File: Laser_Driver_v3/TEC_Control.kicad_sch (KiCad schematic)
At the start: 49 parts, among them Q10 IRF9540N, Q11 IRLB8721PBF, Q12 IRF9540N, Q13 IRLB8721PBF, Q14 IRF9540N, Q7 IRLB8721PBF, Q8 IRF9540N, Q9 IRLB8721PBF, U18 OPA192, U19 OPA192, U20 OPA192, U21 OPA551U, U22 OPA551U

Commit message: Update names, footprints, values, and created BOM
Updated files names, foot prints, component values, parts.
Assigned values from Digikey catalog.
Created CSV BOMs for each schematic.
Including a Power analysis now for all components.
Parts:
- R44, R45, R46, R47, R48, R49, R50, R51, R52, R53, R54, R55, R56, R57, R58, R60: footprint Resistor_SMD:R_0402_1005Metric -> Resistor_SMD:R_0805_2012Metric_Pad1.20x1.40mm_HandSolder
- U18, U19, U20: value OPA192 -> OPA192IDR; footprint Package_SO:SOIC-5-6_4.4x3.6mm_P1.27mm -> Package_SO:SOIC-8_3.9x4.9mm_P1.27mm
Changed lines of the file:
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@@
 			)
 		)
-		(property "Footprint" "Resistor_SMD:R_0402_1005Metric"
+		(property "Footprint" "Resistor_SMD:R_0805_2012Metric_Pad1.20x1.40mm_HandSolder"
 			(at 124.46 140.97 0)
 			(hide yes)
@@
 			)
 		)
-		(property "Footprint" "Resistor_SMD:R_0402_1005Metric"
+		(property "Footprint" "Resistor_SMD:R_0805_2012Metric_Pad1.20x1.40mm_HandSolder"
 			(at 138.43 43.18 0)
 			(hide yes)
@@
 			)
 		)
-		(property "Footprint" "Resistor_SMD:R_0402_1005Metric"
+		(property "Footprint" "Resistor_SMD:R_0805_2012Metric_Pad1.20x1.40mm_HandSolder"
 			(at 124.46 120.65 0)
 			(hide yes)
@@
 			)
 		)
-		(property "Footprint" "Resistor_SMD:R_0402_1005Metric"
+		(property "Footprint" "Resistor_SMD:R_0805_2012Metric_Pad1.20x1.40mm_HandSolder"
 			(at 101.6 57.15 0)
 			(hide yes)
@@
 			)
 		)
-		(property "Footprint" "Resistor_SMD:R_0402_1005Metric"
+		(property "Footprint" "Resistor_SMD:R_0805_2012Metric_Pad1.20x1.40mm_HandSolder"
 			(at 171.45 60.96 0)
 			(hide yes)
@@
 			)
 		)
-		(property "Footprint" "Resistor_SMD:R_0402_1005Metric"
+		(property "Footprint" "Resistor_SMD:R_0805_2012Metric_Pad1.20x1.40mm_HandSolder"
 			(at 124.46 134.62 0)
 			(hide yes)
@@
 			)
 		)
-		(property "Footprint" "Resistor_SMD:R_0402_1005Metric"
+		(property "Footprint" "Resistor_SMD:R_0805_2012Metric_Pad1.20x1.40mm_HandSolder"
 			(at 87.63 134.62 0)
 			(hide yes)
@@
 			)
 		)
-		(property "Value" "OPA192"
+		(property "Value" "OPA192IDR"
 			(at 63.5 129.794 0)
 			(show_name no)
@@
 			)
 		)
-		(property "Footprint" "Package_SO:SOIC-5-6_4.4x3.6mm_P1.27mm"
+		(property "Footprint" "Package_SO:SOIC-8_3.9x4.9mm_P1.27mm"
 			(at 78.486 117.094 0)
 			(hide yes)
@@
 			)
 		)
-		(property "Footprint" "Resistor_SMD:R_0402_1005Metric"
+		(property "Footprint" "Resistor_SMD:R_0805_2012Metric_Pad1.20x1.40mm_HandSolder"
 			(at 114.3 163.83 0)
 			(hide yes)
@@
 			)
 		)
-		(property "Footprint" "Resistor_SMD:R_0402_1005Metric"
+		(property "Footprint" "Resistor_SMD:R_0805_2012Metric_Pad1.20x1.40mm_HandSolder"
 			(at 138.43 49.53 0)
 			(hide yes)
@@
 			)
 		)
-		(property "Value" "OPA192"
+		(property "Value" "OPA192IDR"
 			(at 77.47 52.324 0)
 			(show_name no)
@@
 			)
 		)
-		(property "Footprint" "Package_SO:SOIC-5-6_4.4x3.6mm_P1.27mm"
+		(property "Footprint" "Package_SO:SOIC-8_3.9x4.9mm_P1.27mm"
 			(at 92.456 39.624 0)
 			(hide yes)
@@
 			)
 		)
-		(property "Footprint" "Resistor_SMD:R_0402_1005Metric"
+		(property "Footprint" "Resistor_SMD:R_0805_2012Metric_Pad1.20x1.40mm_HandSolder"
 			(at 128.27 86.36 0)
 			(hide yes)
@@
 			)
 		)
-		(property "Footprint" "Resistor_SMD:R_0402_1005Metric"
+		(property "Footprint" "Resistor_SMD:R_0805_2012Metric_Pad1.20x1.40mm_HandSolder"
 			(at 138.43 57.15 0)
 			(hide yes)
@@
 			)
 		)
-		(property "Footprint" "Resistor_SMD:R_0402_1005Metric"
+		(property "Footprint" "Resistor_SMD:R_0805_2012Metric_Pad1.20x1.40mm_HandSolder"
 			(at 100.33 163.83 0)
 			(hide yes)
@@
 			)
 		)
-		(property "Footprint" "Resistor_SMD:R_0402_1005Metric"
+		(property "Footprint" "Resistor_SMD:R_0805_2012Metric_Pad1.20x1.40mm_HandSolder"
 			(at 114.3 86.36 0)
 			(hide yes)
@@
 			)
 		)
-		(property "Footprint" "Resistor_SMD:R_0402_1005Metric"
+		(property "Footprint" "Resistor_SMD:R_0805_2012Metric_Pad1.20x1.40mm_HandSolder"
 			(at 157.48 138.43 0)
 			(hide yes)
@@
 			)
 		)
-		(property "Value" "OPA192"
+		(property "Value" "OPA192IDR"
 			(at 43.18 82.804 0)
 			(show_name no)
@@
 			)
 		)
-		(property "Footprint" "Package_SO:SOIC-5-6_4.4x3.6mm_P1.27mm"
+		(property "Footprint" "Package_SO:SOIC-8_3.9x4.9mm_P1.27mm"
 			(at 58.166 70.104 0)
 			(hide yes)
@@
 			)
 		)
-		(property "Footprint" "Resistor_SMD:R_0402_1005Metric"
+		(property "Footprint" "Resistor_SMD:R_0805_2012Metric_Pad1.20x1.40mm_HandSolder"
 			(at 138.43 63.5 0)
 			(hide yes)
@@
 			)
 		)
-		(property "Footprint" "Resistor_SMD:R_0402_1005Metric"
+		(property "Footprint" "Resistor_SMD:R_0805_2012Metric_Pad1.20x1.40mm_HandSolder"
 			(at 124.46 127 0)
 			(hide yes)

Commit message: Clearing ERC errors. laying out components.
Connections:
- net +6V_TEC: now also Q13.2 (D)
- net -6V_TEC: now also Q14.3 (S)
- net at Q13.1 (G), R54.2: now also D21.2 (A)
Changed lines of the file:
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@@
+	)
+	(junction
+		(at 200.66 40.64)
+		(diameter 0)
+		(color 0 0 0 0)
+	)
+	(junction
+		(at 200.66 76.2)
+		(diameter 0)
+		(color 0 0 0 0)
 	)
 	(junction
@@
 	)
 	(junction
+		(at 213.36 49.53)
+		(diameter 0)
+		(color 0 0 0 0)
+	)
+	(junction
 		(at 118.11 127)
 		(diameter 0)
@@
 	)
 	(junction
+		(at 160.02 153.67)
+		(diameter 0)
+		(color 0 0 0 0)
+	)
+	(junction
+		(at 195.58 127)
+		(diameter 0)
+		(color 0 0 0 0)
+	)
+	(junction
+		(at 160.02 118.11)
+		(diameter 0)
+		(color 0 0 0 0)
+	)
+	(junction
+		(at 186.69 134.62)
+		(diameter 0)
+		(color 0 0 0 0)
+	)
+	(junction
+		(at 73.66 149.86)
+		(diameter 0)
+		(color 0 0 0 0)
+	)
+	(junction
+		(at 135.89 127)
+		(diameter 0)
+		(color 0 0 0 0)
+	)
+	(junction
+		(at 144.78 134.62)
+		(diameter 0)
+		(color 0 0 0 0)
+	)
+	(junction
+		(at 149.86 49.53)
+		(diameter 0)
+		(color 0 0 0 0)
+	)
+	(junction
+		(at 209.55 64.77)
+		(diameter 0)
+		(color 0 0 0 0)
+	)
+	(junction
+		(at 132.08 59.69)
+		(diameter 0)
+		(color 0 0 0 0)
+	)
+	(junction
+		(at 60.96 87.63)
+		(diameter 0)
+		(color 0 0 0 0)
+	)
+	(junction
+		(at 186.69 118.11)
+		(diameter 0)
+		(color 0 0 0 0)
+	)
+	(junction
+		(at 147.32 64.77)
+		(diameter 0)
+		(color 0 0 0 0)
+	)
+	(junction
+		(at 132.08 49.53)
+		(diameter 0)
+		(color 0 0 0 0)
+	)
+	(junction
 		(at 175.26 76.2)
 		(diameter 0)
@@
 	)
 	(junction
-		(at 160.02 153.67)
-		(diameter 0)
-		(color 0 0 0 0)
-	)
-	(junction
-		(at 195.58 127)
-		(diameter 0)
-		(color 0 0 0 0)
-	)
-	(junction
-		(at 160.02 118.11)
-		(diameter 0)
-		(color 0 0 0 0)
-	)
-	(junction
-		(at 186.69 134.62)
-		(diameter 0)
-		(color 0 0 0 0)
-	)
-	(junction
-		(at 73.66 149.86)
-		(diameter 0)
-		(color 0 0 0 0)
-	)
-	(junction
-		(at 135.89 127)
-		(diameter 0)
-		(color 0 0 0 0)
-	)
-	(junction
-		(at 144.78 134.62)
-		(diameter 0)
-		(color 0 0 0 0)
-	)
-	(junction
-		(at 149.86 49.53)
-		(diameter 0)
-		(color 0 0 0 0)
-	)
-	(junction
-		(at 209.55 64.77)
-		(diameter 0)
-		(color 0 0 0 0)
-	)
-	(junction
-		(at 132.08 59.69)
-		(diameter 0)
-		(color 0 0 0 0)
-	)
-	(junction
-		(at 60.96 87.63)
-		(diameter 0)
-		(color 0 0 0 0)
-	)
-	(junction
-		(at 186.69 118.11)
-		(diameter 0)
-		(color 0 0 0 0)
-	)
-	(junction
-		(at 147.32 64.77)
-		(diameter 0)
-		(color 0 0 0 0)
-	)
-	(junction
-		(at 132.08 49.53)
-		(diameter 0)
-		(color 0 0 0 0)
-	)
-	(junction
 		(at 73.66 120.65)
 		(diameter 0)
@@
 	(wire
 		(pts
-			(xy 200.66 44.45) (xy 200.66 40.64)
-		)
-		(stroke
-			(width 0)
-			(type default)
-		)
-	)
-	(wire
-		(pts
 			(xy 31.75 90.17) (xy 31.75 91.44)
 		)
@@
 	(wire
 		(pts
+			(xy 200.66 40.64) (xy 213.36 40.64)
+		)
+		(stroke
+			(width 0)
+			(type default)
+		)
+	)
+	(wire
+		(pts
 			(xy 195.58 152.4) (xy 195.58 154.94)
 		)
@@
 	(wire
 		(pts
-			(xy 175.26 76.2) (xy 209.55 76.2)
+			(xy 175.26 76.2) (xy 200.66 76.2)
 		)
 		(stroke
@@
 	(wire
 		(pts
+			(xy 200.66 40.64) (xy 200.66 44.45)
+		)
+		(stroke
+			(width 0)
+			(type default)
+		)
+	)
+	(wire
+		(pts
 			(xy 160.02 151.13) (xy 160.02 153.67)
 		)
@@
 	(wire
 		(pts
-			(xy 172.72 40.64) (xy 213.36 40.64)
+			(xy 172.72 40.64) (xy 200.66 40.64)
 		)
 		(stroke
@@
 	(wire
 		(pts
+			(xy 213.36 49.53) (xy 219.71 49.53)
+		)
+		(stroke
+			(width 0)
+			(type default)
+		)
+	)
+	(wire
+		(pts
+			(xy 200.66 76.2) (xy 209.55 76.2)
+		)
+		(stroke
+			(width 0)
+			(type default)
+		)
+	)
+	(wire
+		(pts
 			(xy 171.45 64.77) (xy 176.53 64.77)
 		)
@@
 	(wire
 		(pts
-			(xy 208.28 49.53) (xy 219.71 49.53)
-		)
-		(stroke
+			(xy 208.28 49.53) (xy 213.36 49.53)
+		)
+		(stroke

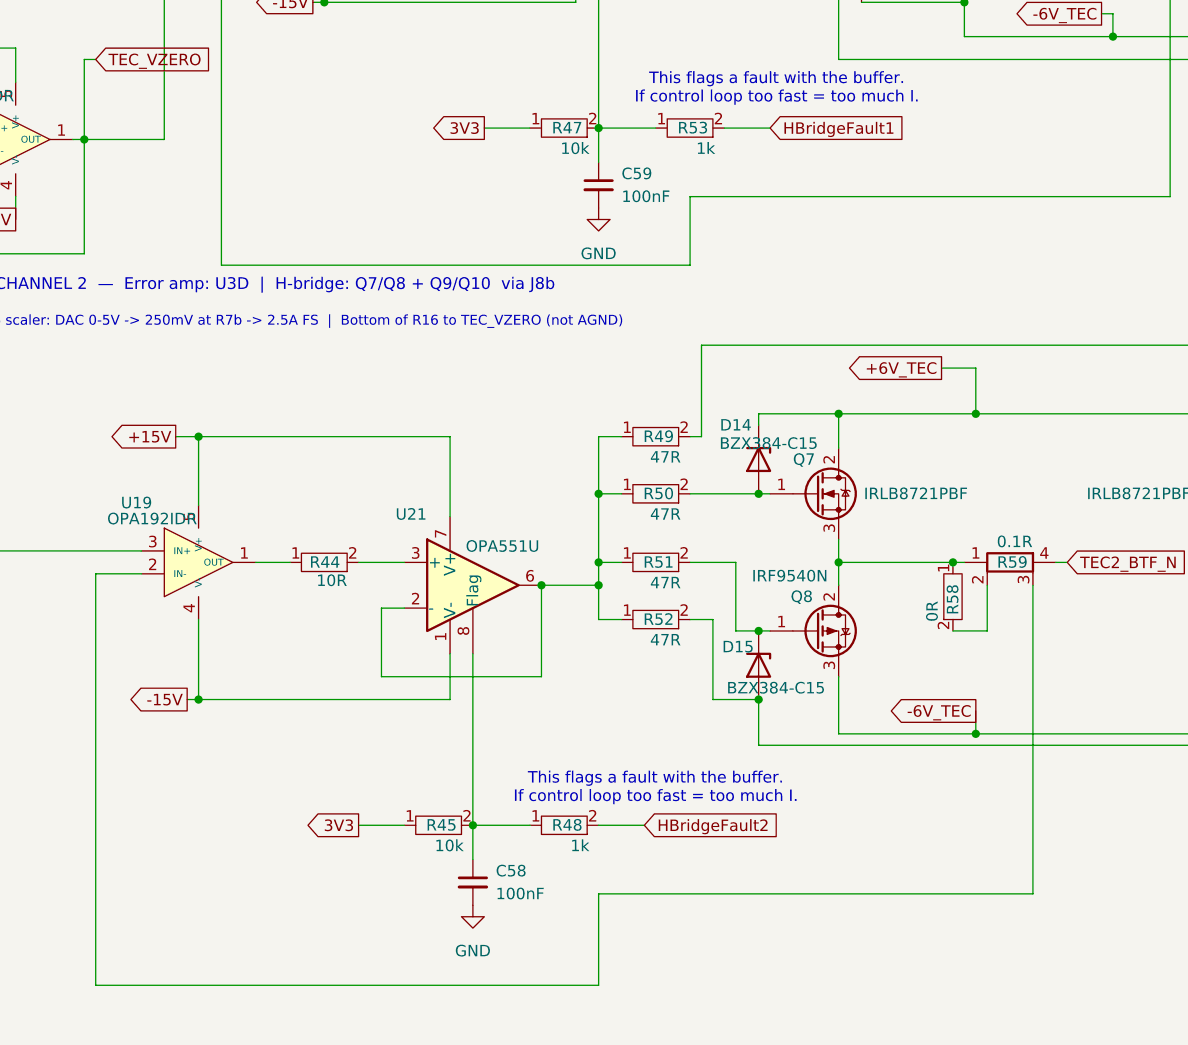
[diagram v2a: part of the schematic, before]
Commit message: Added separate xfrmer for 6V.
Added inrush protection with NTC and increased capacitance to reduce ripple on 6V
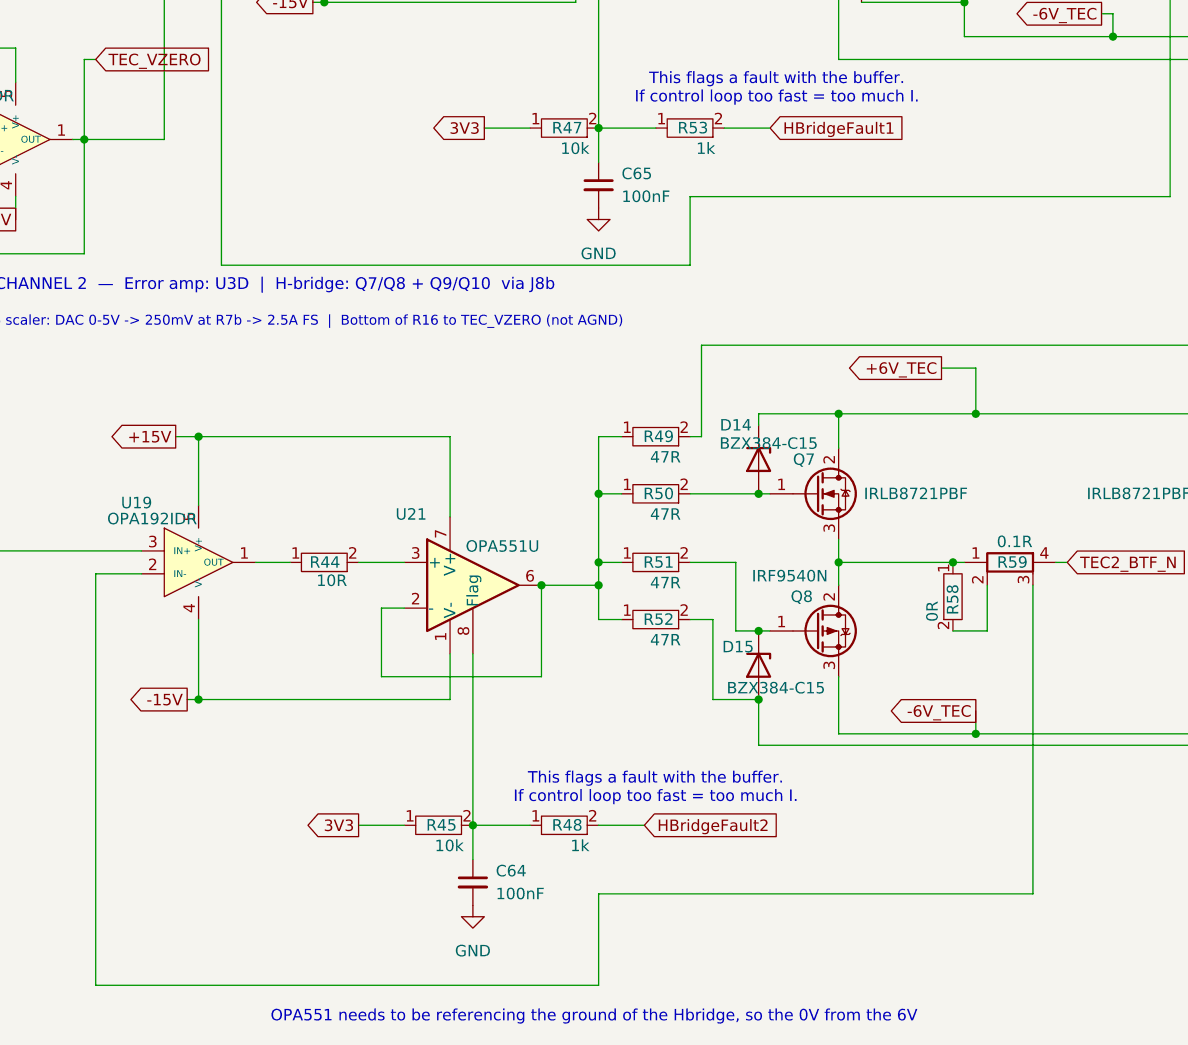
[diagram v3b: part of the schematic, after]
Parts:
- renumbered C58 to C64, C59 to C65
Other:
- note added: "OPA551 needs to be referencing the ground of the Hbridge, so the 0V from the 6V"
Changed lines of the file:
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@@
 		)
 	)
+	(text "OPA551 needs to be referencing the ground of the Hbridge, so the 0V from the 6V"
+		(exclude_from_sim no)
+		(at 117.602 185.166 0)
+		(effects
+			(font
+				(size 1.27 1.27)
+			)
+		)
+	)
 	(text "TEC CHANNEL 2  —  Error amp: U3D  |  H-bridge: Q7/Q8 + Q9/Q10  via J8b"
 		(exclude_from_sim no)
@@
 		(in_pos_files yes)
 		(dnp no)
-		(property "Reference" "#PWR017"
+		(property "Reference" "#PWR020"
 			(at 31.75 105.41 0)
 			(hide yes)
@@
 			(project "laser_driver_v3"
 				(path "/b2c3d4e5-f6a7-8901-bcde-f12345678901/06f22b47-dee6-4fbe-8e7e-6abe24fabe38"
-					(reference "#PWR017")
+					(reference "#PWR020")
 					(unit 1)
 				)
@@
 		(dnp no)
 		(fields_autoplaced yes)
-		(property "Reference" "#PWR019"
+		(property "Reference" "#PWR022"
 			(at 118.11 101.6 0)
 			(hide yes)
@@
 			(project "laser_driver_v3"
 				(path "/b2c3d4e5-f6a7-8901-bcde-f12345678901/06f22b47-dee6-4fbe-8e7e-6abe24fabe38"
-					(reference "#PWR019")
+					(reference "#PWR022")
 					(unit 1)
 				)
@@
 		(dnp no)
 		(fields_autoplaced yes)
-		(property "Reference" "C59"
+		(property "Reference" "C65"
 			(at 120.65 91.4462 0)
 			(show_name no)
@@
 			(project "laser_driver_v3"
 				(path "/b2c3d4e5-f6a7-8901-bcde-f12345678901/06f22b47-dee6-4fbe-8e7e-6abe24fabe38"
-					(reference "C59")
+					(reference "C65")
 					(unit 1)
 				)
@@
 		(dnp no)
 		(fields_autoplaced yes)
-		(property "Reference" "#PWR018"
+		(property "Reference" "#PWR021"
 			(at 104.14 179.07 0)
 			(hide yes)
@@
 			(project "laser_driver_v3"
 				(path "/b2c3d4e5-f6a7-8901-bcde-f12345678901/06f22b47-dee6-4fbe-8e7e-6abe24fabe38"
-					(reference "#PWR018")
+					(reference "#PWR021")
 					(unit 1)
 				)
@@
 		(dnp no)
 		(fields_autoplaced yes)
-		(property "Reference" "C58"
+		(property "Reference" "C64"
 			(at 106.68 168.9162 0)
 			(show_name no)
@@
 			(project "laser_driver_v3"
 				(path "/b2c3d4e5-f6a7-8901-bcde-f12345678901/06f22b47-dee6-4fbe-8e7e-6abe24fabe38"
-					(reference "C58")
+					(reference "C64")
 					(unit 1)
 				)

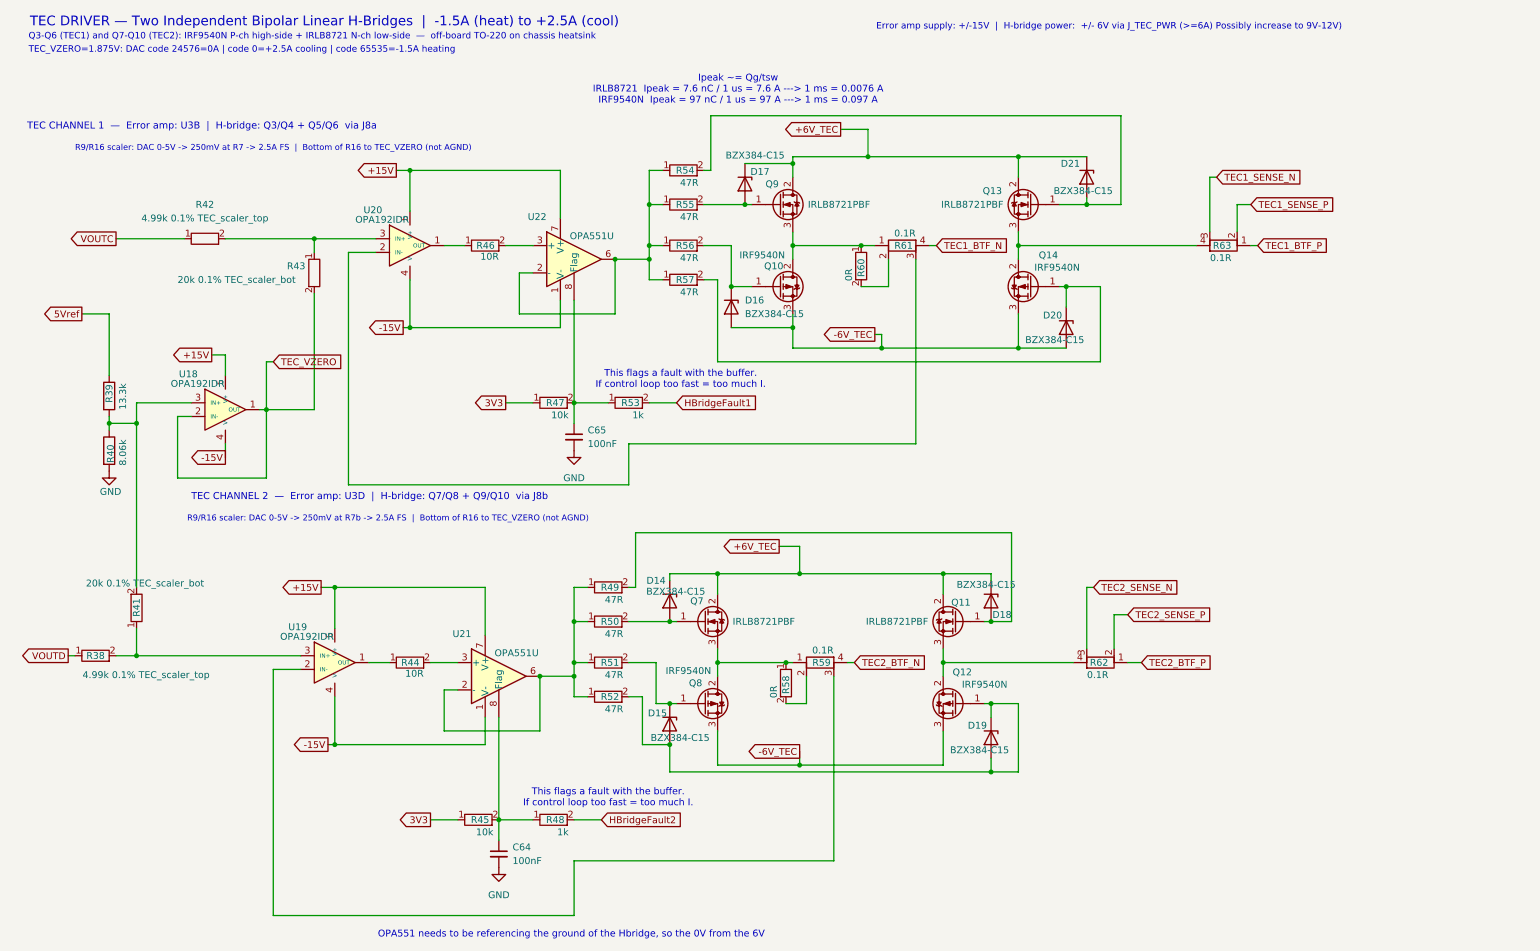
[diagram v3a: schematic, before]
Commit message: Changed xfrmers, paralled BJTs for cap multiplier
Changed the transformers to more appropriate voltages.
Made the BJTs for the cap multipliers in parallel to better handle the load.
Simulated the output ripple for the 6V.
Clarifying notes, removed LT1028 changed to OPA192 to match circuit as drawn.
Changed divider values for the TEC_zero value to be 1.2 V as designed.
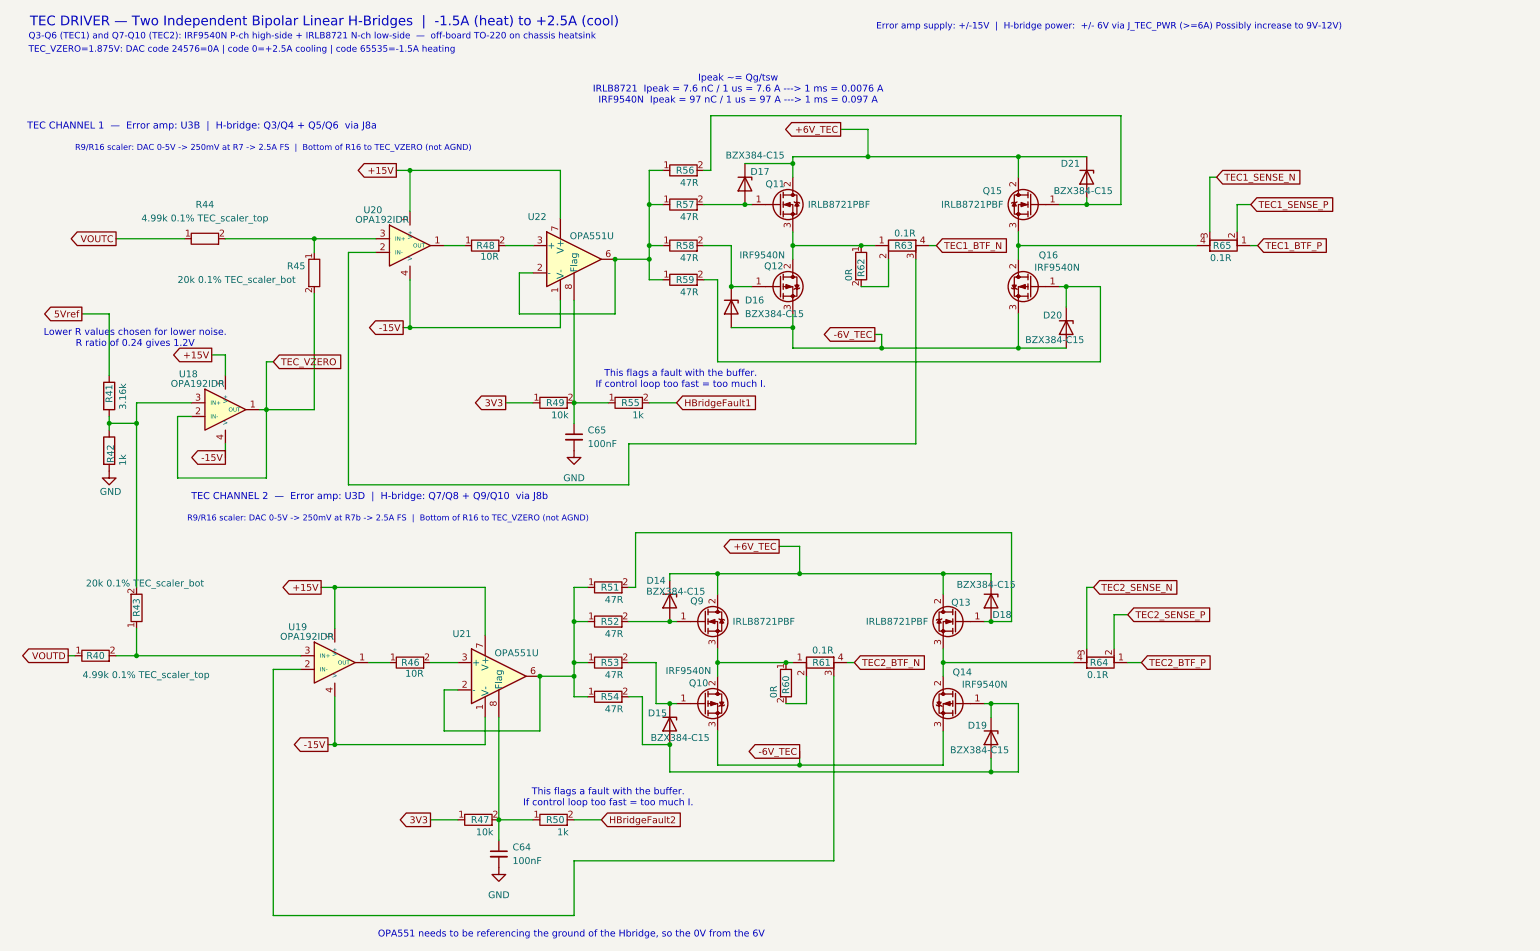
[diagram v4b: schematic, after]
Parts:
- R41: renamed from R39; value 13.3k -> 3.16k
- R42: renamed from R40; value 8.06k -> 1k
- renumbered Q8 to Q10, Q9 to Q11, Q10 to Q12, Q11 to Q13, Q12 to Q14, Q13 to Q15, Q14 to Q16, Q7 to Q9, R38 to R40, R41 to R43, R42 to R44, R43 to R45, R44 to R46, R45 to R47, R46 to R48, R47 to R49, R48 to R50, R49 to R51, R50 to R52, R51 to R53, R52 to R54, R53 to R55, R54 to R56, R55 to R57, R56 to R58, R57 to R59, R58 to R60, R59 to R61, R60 to R62, R61 to R63, R62 to R64, R63 to R65
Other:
- note added: "Lower R values chosen for lower noise. R ratio of 0.24 gives 1.2V"
